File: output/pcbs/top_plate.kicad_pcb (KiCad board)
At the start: 2 copper layers, 162.1 x 157 mm, 58 parts

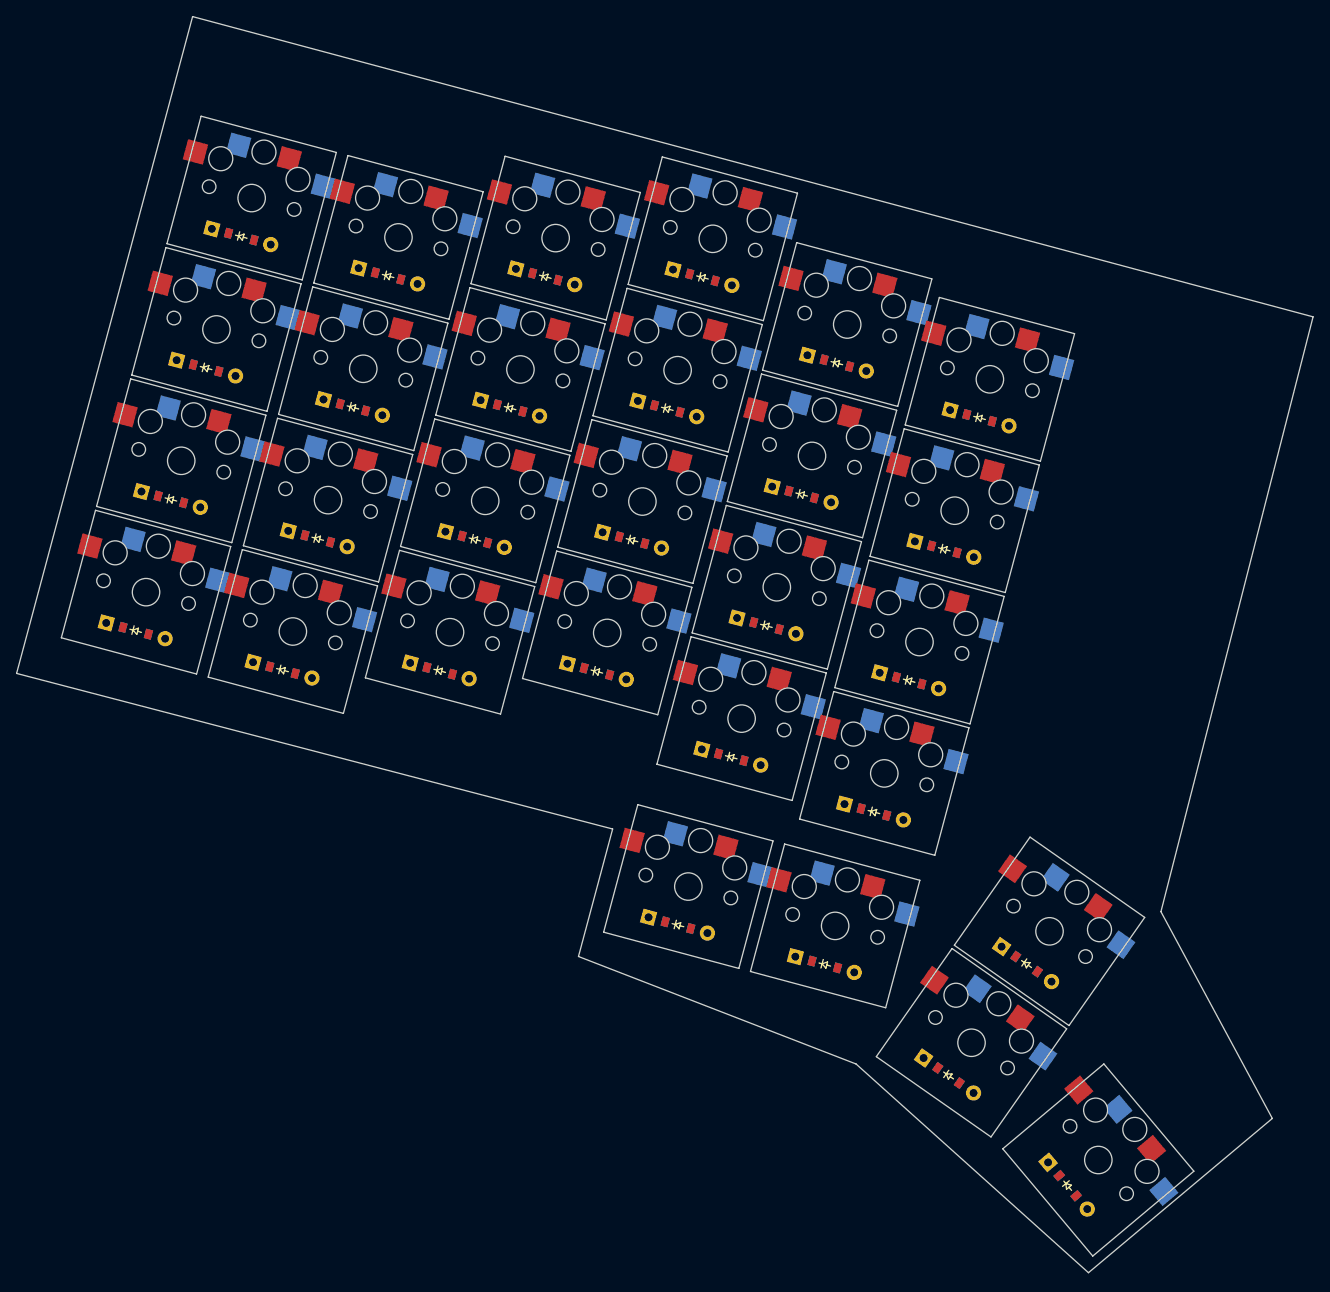
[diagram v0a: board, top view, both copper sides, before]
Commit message: v4 migration complete
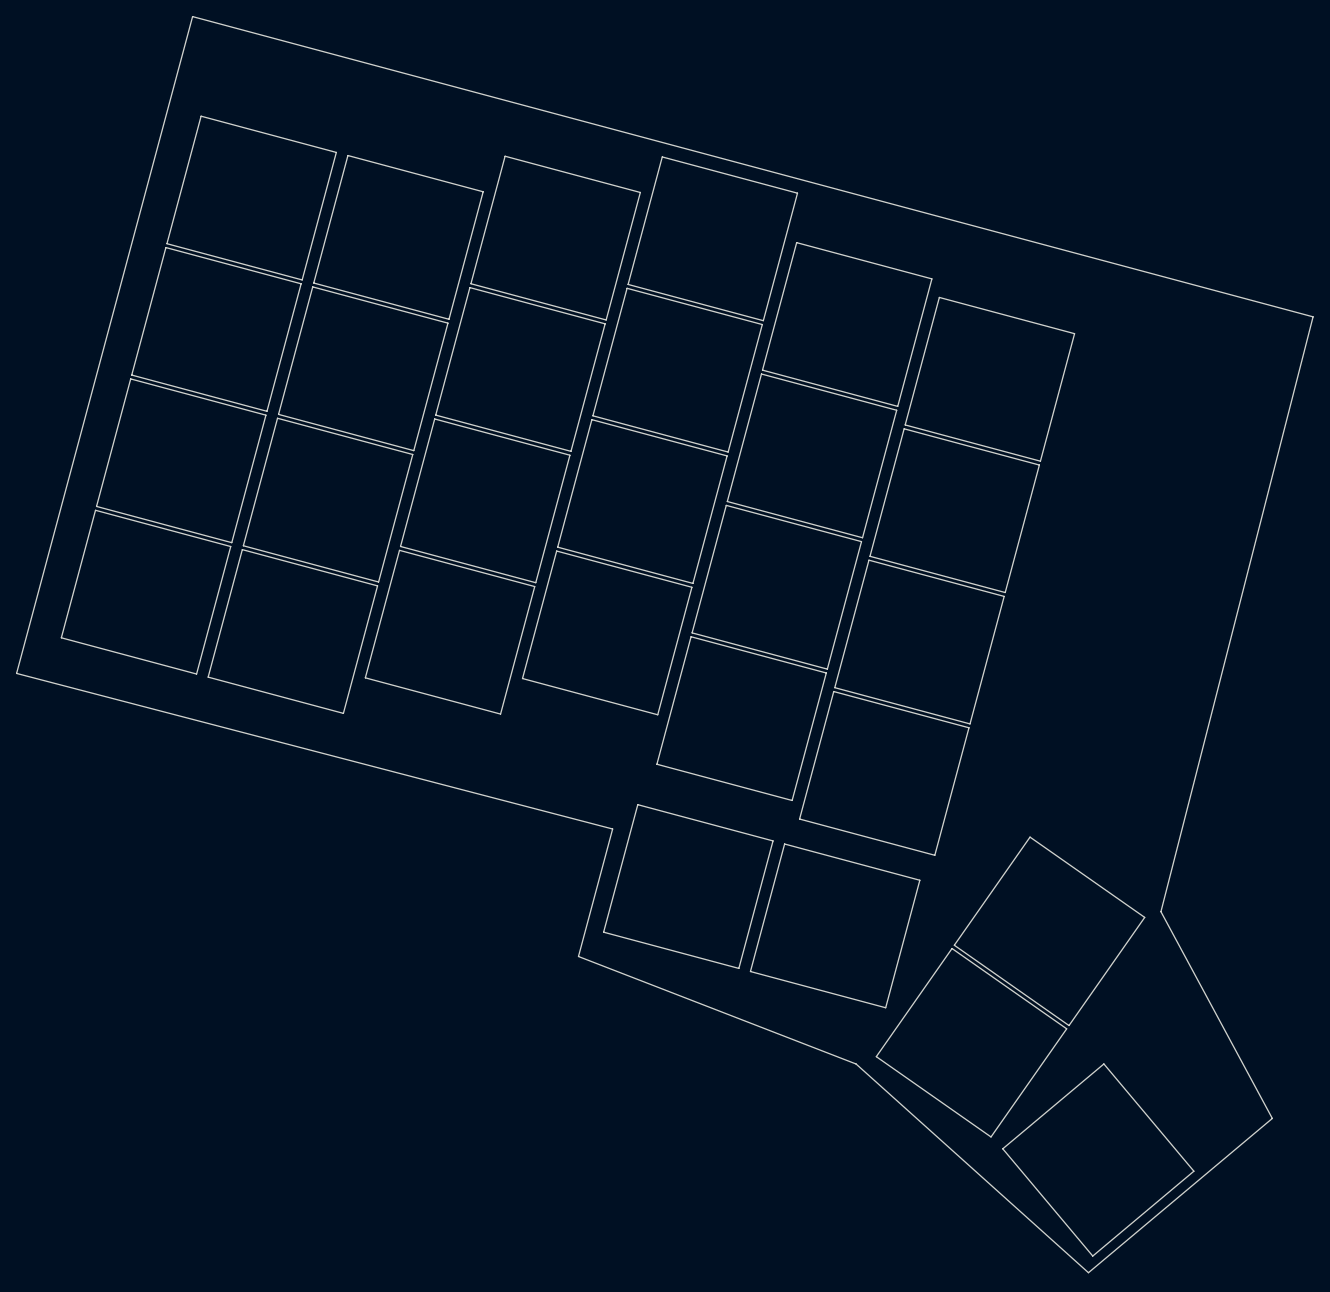
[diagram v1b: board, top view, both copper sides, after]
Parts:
- removed D1, D10, D11, D12, D13, D14, D15, D16, D17, D18, D19, D2, D20, D21, D22, D23, D24, D25, D26, D27, D28, D29, D3, D4, D5, D6, D7, D8, D9: , ComboDiode
- removed S1, S10, S11, S12, S13, S14, S15, S16, S17, S18, S19, S2, S20, S21, S22, S23, S24, S25, S26, S27, S28, S29, S3, S4, S5, S6, S7, S8, S9: , PG1350

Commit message: holes
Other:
- board size 162.1 x 157 mm -> 161.8 x 156.7 mm
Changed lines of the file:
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@@
     (add_net "")
   )
-            (gr_line (start -16.1805024 10.158314) (end 5.819116599999999 -71.94538130000001) (angle 90) (layer Edge.Cuts) (width 0.15))
-(gr_line (start 5.819116599999999 -71.94538130000001) (end 145.87836140000002 -34.4166198) (angle 90) (layer Edge.Cuts) (width 0.15))
-(gr_line (start 145.87836140000002 -34.4166198) (end 126.8621417 39.9409735) (angle 90) (layer Edge.Cuts) (width 0.15))
-(gr_line (start 126.8621417 39.9409735) (end 140.7847307 65.7853827) (angle 90) (layer Edge.Cuts) (width 0.15))
-(gr_line (start 140.7847307 65.7853827) (end 117.80339740000001 85.06901099999999) (angle 90) (layer Edge.Cuts) (width 0.15))
-(gr_line (start 117.80339740000001 85.06901099999999) (end 88.758661 58.982201599999996) (angle 90) (layer Edge.Cuts) (width 0.15))
-(gr_line (start 88.758661 58.982201599999996) (end 54.054681599999995 45.5421936) (angle 90) (layer Edge.Cuts) (width 0.15))
-(gr_line (start 54.054681599999995 45.5421936) (end 58.325195799999996 29.604417499999997) (angle 90) (layer Edge.Cuts) (width 0.15))
-(gr_line (start 58.325195799999996 29.604417499999997) (end -16.1805024 10.158314) (angle 90) (layer Edge.Cuts) (width 0.15))
+            (gr_line (start -16.050249842682216 9.672204841561154) (end 5.6897070767034235 -71.46241838733955) (angle 90) (layer Edge.Cuts) (width 0.15))
+(gr_line (start 6.302079476703429 -71.81597178733956) (end 145.400885349558 -34.54455912199612) (angle 90) (layer Edge.Cuts) (width 0.15))
+(gr_line (start 145.75588576462945 -33.93771318092877) (end 126.91051278171823 39.75183195248809) (angle 90) (layer Edge.Cuts) (width 0.15))
+(gr_line (start 126.95473240803616 40.11284901443227) (end 140.59163301925636 65.42693676176896) (angle 90) (layer Edge.Cuts) (width 0.15))
+(gr_line (start 140.47283653050286 66.04709298264581) (end 118.13593657307975 84.78997750245881) (angle 90) (layer Edge.Cuts) (width 0.15))
+(gr_line (start 117.48043880075463 84.77894262731525) (end 88.82679495778186 59.04339676961162) (angle 90) (layer Edge.Cuts) (width 0.15))
+(gr_line (start 88.67326060229512 58.94912810098919) (end 54.47324822304958 45.70429428296431) (angle 90) (layer Edge.Cuts) (width 0.15))
+(gr_line (start 54.17085493988792 45.10862878948538) (end 58.19494324450718 30.090526658915167) (angle 90) (layer Edge.Cuts) (width 0.15))
+(gr_line (start 57.83825107910054 29.477324167944097) (end -15.69355767727557 10.285407332532225) (angle 90) (layer Edge.Cuts) (width 0.15))
+(gr_arc (start 6.172669976703426 -71.33300888733956) (end 6.302079476703426 -71.81597178733956) (angle -90.00000000000094) (layer Edge.Cuts) (width 0.15))
+(gr_arc (start 145.27147584955802 -34.06159622199612) (end 145.75588574955802 -33.93771322199612) (angle -89.34536259454504) (layer Edge.Cuts) (width 0.15))
+(gr_arc (start 127.39492269678965 39.87571499355545) (end 126.91051279678965 39.75183199355545) (angle -42.65706137359828) (layer Edge.Cuts) (width 0.15))
+(gr_arc (start 140.15144273050288 65.66407078264578) (end 140.4728365305029 66.04709298264578) (angle -78.31169972246471) (layer Edge.Cuts) (width 0.15))
+(gr_arc (start 117.81454277307972 84.40695530245878) (end 117.48043887307972 84.77894260245878) (angle -81.92890097930959) (layer Edge.Cuts) (width 0.15))
+(gr_arc (start 88.49269098545678 59.41538409446811) (end 88.82679488545678 59.04339679446811) (angle -20.75872474796588) (layer Edge.Cuts) (width 0.15))
+(gr_arc (start 54.65381783988792 45.23803828948539) (end 54.170854939887924 45.10862878948539) (angle -83.82982282525415) (layer Edge.Cuts) (width 0.15))
+(gr_arc (start 57.71198034450719 29.961117158915158) (end 58.194943244507186 30.09052665891516) (angle -90.37204223967748) (layer Edge.Cuts) (width 0.15))
+(gr_arc (start -15.567286942682214 9.801614341561148) (end -16.050249842682213 9.672204841561149) (angle -90.37204223967527) (layer Edge.Cuts) (width 0.15))
 (gr_line (start -10.5871081 5.7042214) (end 6.316593900000001 10.2335547) (angle 90) (layer Edge.Cuts) (width 0.15))
 (gr_line (start 6.316593900000001 10.2335547) (end 10.587108100000002 -5.7042214) (angle 90) (layer Edge.Cuts) (width 0.15))

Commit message: new onoff and placements
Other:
- board size 161.8 x 156.7 mm -> 161.4 x 156.2 mm
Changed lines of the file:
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@@
     (add_net "")
   )
-            (gr_line (start -16.050249842682216 9.672204841561154) (end 5.6897070767034235 -71.46241838733955) (angle 90) (layer Edge.Cuts) (width 0.15))
-(gr_line (start 6.302079476703429 -71.81597178733956) (end 145.400885349558 -34.54455912199612) (angle 90) (layer Edge.Cuts) (width 0.15))
-(gr_line (start 145.75588576462945 -33.93771318092877) (end 126.91051278171823 39.75183195248809) (angle 90) (layer Edge.Cuts) (width 0.15))
-(gr_line (start 126.95473240803616 40.11284901443227) (end 140.59163301925636 65.42693676176896) (angle 90) (layer Edge.Cuts) (width 0.15))
-(gr_line (start 140.47283653050286 66.04709298264581) (end 118.13593657307975 84.78997750245881) (angle 90) (layer Edge.Cuts) (width 0.15))
-(gr_line (start 117.48043880075463 84.77894262731525) (end 88.82679495778186 59.04339676961162) (angle 90) (layer Edge.Cuts) (width 0.15))
-(gr_line (start 88.67326060229512 58.94912810098919) (end 54.47324822304958 45.70429428296431) (angle 90) (layer Edge.Cuts) (width 0.15))
-(gr_line (start 54.17085493988792 45.10862878948538) (end 58.19494324450718 30.090526658915167) (angle 90) (layer Edge.Cuts) (width 0.15))
-(gr_line (start 57.83825107910054 29.477324167944097) (end -15.69355767727557 10.285407332532225) (angle 90) (layer Edge.Cuts) (width 0.15))
-(gr_arc (start 6.172669976703426 -71.33300888733956) (end 6.302079476703426 -71.81597178733956) (angle -90.00000000000094) (layer Edge.Cuts) (width 0.15))
-(gr_arc (start 145.27147584955802 -34.06159622199612) (end 145.75588574955802 -33.93771322199612) (angle -89.34536259454504) (layer Edge.Cuts) (width 0.15))
-(gr_arc (start 127.39492269678965 39.87571499355545) (end 126.91051279678965 39.75183199355545) (angle -42.65706137359828) (layer Edge.Cuts) (width 0.15))
-(gr_arc (start 140.15144273050288 65.66407078264578) (end 140.4728365305029 66.04709298264578) (angle -78.31169972246471) (layer Edge.Cuts) (width 0.15))
-(gr_arc (start 117.81454277307972 84.40695530245878) (end 117.48043887307972 84.77894260245878) (angle -81.92890097930959) (layer Edge.Cuts) (width 0.15))
-(gr_arc (start 88.49269098545678 59.41538409446811) (end 88.82679488545678 59.04339679446811) (angle -20.75872474796588) (layer Edge.Cuts) (width 0.15))
-(gr_arc (start 54.65381783988792 45.23803828948539) (end 54.170854939887924 45.10862878948539) (angle -83.82982282525415) (layer Edge.Cuts) (width 0.15))
-(gr_arc (start 57.71198034450719 29.961117158915158) (end 58.194943244507186 30.09052665891516) (angle -90.37204223967748) (layer Edge.Cuts) (width 0.15))
-(gr_arc (start -15.567286942682214 9.801614341561148) (end -16.050249842682213 9.672204841561149) (angle -90.37204223967527) (layer Edge.Cuts) (width 0.15))
+            (gr_line (start -15.750826166054502 4.691037439738906) (end 3.2096897053102573 -66.07057118109151) (angle 90) (layer Edge.Cuts) (width 0.15))
+(gr_line (start 10.98681946566925 -70.56069952295685) (end 140.75644270033658 -35.78903371992137) (angle 90) (layer Edge.Cuts) (width 0.15))
+(gr_line (start 145.25871255989853 -28.057905348812596) (end 128.5974752815291 36.039867943558875) (angle 90) (layer Edge.Cuts) (width 0.15))
+(gr_line (start 129.0289030206753 40.406624515045564) (end 139.94800963870154 62.93812754589385) (angle 90) (layer Edge.Cuts) (width 0.15))
+(gr_line (start 138.39328511725896 70.50530891686543) (end 123.01848155492726 83.83467946748286) (angle 90) (layer Edge.Cuts) (width 0.15))
+(gr_line (start 114.46492165559799 83.62105216067538) (end 89.74926410731214 59.93167154636846) (angle 90) (layer Edge.Cuts) (width 0.15))
+(gr_line (start 87.46441016933812 58.526456807326745) (end 57.244283869904265 47.885037950479905) (angle 90) (layer Edge.Cuts) (width 0.15))
+(gr_line (start 53.17277647630275 40.43856199702745) (end 54.22868411828011 35.959292193949324) (angle 90) (layer Edge.Cuts) (width 0.15))
+(gr_line (start 49.650934570850715 28.35794933985892) (end -11.220042614249925 12.478916601339106) (angle 90) (layer Edge.Cuts) (width 0.15))
+(gr_arc (start 9.343318756422416 -64.42707047184469) (end 10.986819456422417 -70.56069957184468) (angle -90.00000000000007) (layer Edge.Cuts) (width 0.15))
+(gr_arc (start 139.11294199108983 -29.655404668809204) (end 145.25871259108982 -28.057905368809205) (angle -89.57071627961162) (layer Edge.Cuts) (width 0.15))
+(gr_arc (start 134.74324585033784 37.63736726355535) (end 128.59747525033785 36.039867963555345) (angle -40.42624664500161) (layer Edge.Cuts) (width 0.15))
+(gr_arc (start 134.23366680903905 65.70738479738412) (end 138.39328510903906 70.50530889738413) (angle -74.93148460646199) (layer Edge.Cuts) (width 0.15))
+(gr_arc (start 118.8588632467074 79.0367553480016) (end 114.4649216467074 83.62105214800161) (angle -84.70945358480779) (layer Edge.Cuts) (width 0.15))
+(gr_arc (start 85.35532251620273 64.51596835904222) (end 89.74926411620274 59.93167155904222) (angle -24.386702087717396) (layer Edge.Cuts) (width 0.15))
+(gr_arc (start 59.3533715230397 41.89552639876446) (end 53.1727765230397 40.43856199876446) (angle -83.86558988875632) (layer Edge.Cuts) (width 0.15))
+(gr_arc (start 48.04808907154315 34.50232779221233) (end 54.22868407154316 35.959292192212324) (angle -88.64373240863068) (layer Edge.Cuts) (width 0.15))
+(gr_arc (start -9.617197114942343 6.3345381489857235) (end -15.750826214942343 4.691037448985724) (angle -90.37943678171396) (layer Edge.Cuts) (width 0.15))
 (gr_line (start -10.5871081 5.7042214) (end 6.316593900000001 10.2335547) (angle 90) (layer Edge.Cuts) (width 0.15))
 (gr_line (start 6.316593900000001 10.2335547) (end 10.587108100000002 -5.7042214) (angle 90) (layer Edge.Cuts) (width 0.15))
@@
 (gr_line (start 130.9802239 72.3805816) (end 119.7314408 58.9748038) (angle 90) (layer Edge.Cuts) (width 0.15))
 (gr_line (start 119.7314408 58.9748038) (end 107.09170750000001 69.58079939999999) (angle 90) (layer Edge.Cuts) (width 0.15))
+(gr_circle (center 9.985040699999999 -65.0833425) (end 11.0350407 -65.0833425) (layer Edge.Cuts) (width 0.15))
+(gr_circle (center 114.5179052 -37.3844288) (end 115.5679052 -37.3844288) (layer Edge.Cuts) (width 0.15))
+(gr_circle (center -12.3566173 7.8648607) (end -11.3066173 7.8648607) (layer Edge.Cuts) (width 0.15))
+(gr_circle (center 83.1844661 52.778093999999996) (end 84.23446609999999 52.778093999999996) (layer Edge.Cuts) (width 0.15))
+(gr_circle (center 55.843387099999994 25.730062699999998) (end 56.89338709999999 25.730062699999998) (layer Edge.Cuts) (width 0.15))
+(gr_circle (center 136.1658818 66.0059167) (end 137.2158818 66.0059167) (layer Edge.Cuts) (width 0.15))
 )
